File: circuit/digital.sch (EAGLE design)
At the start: 34 parts, among them IC1 MCP1701-5V, IC2 MCP1700-3.3V, X1 MINI-USB-SCHIELD-32005-301

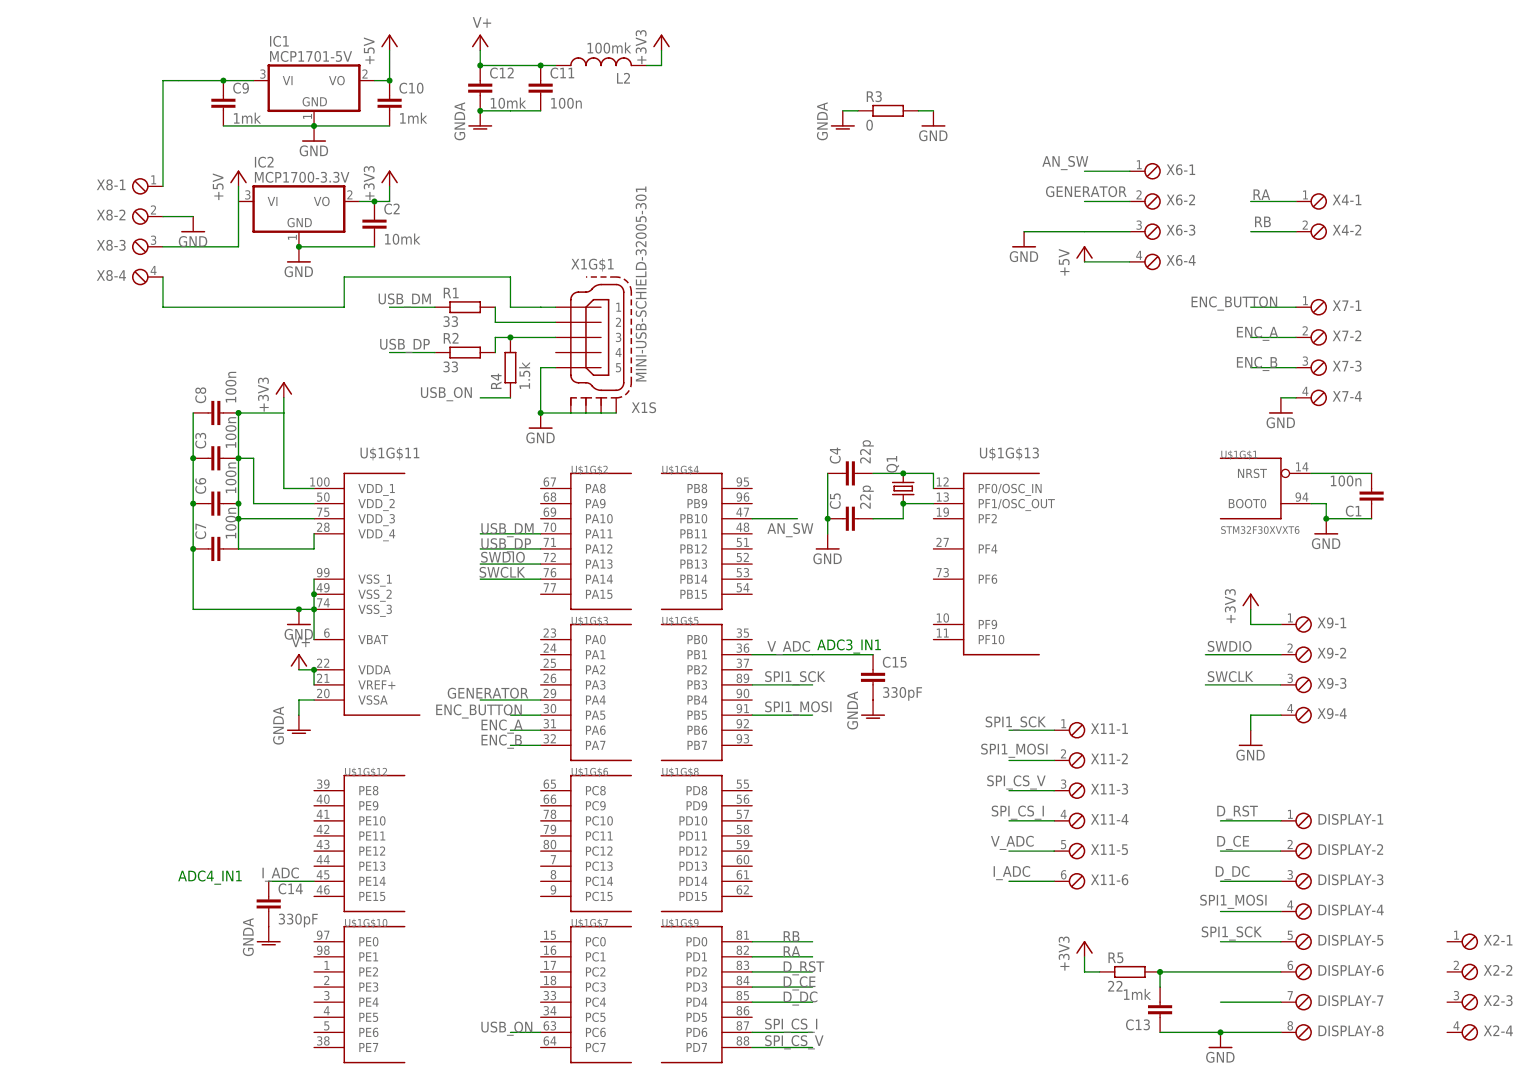
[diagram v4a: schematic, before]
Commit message: - слили вместе GND и GNDA - добавили измерение VBAT напряжения
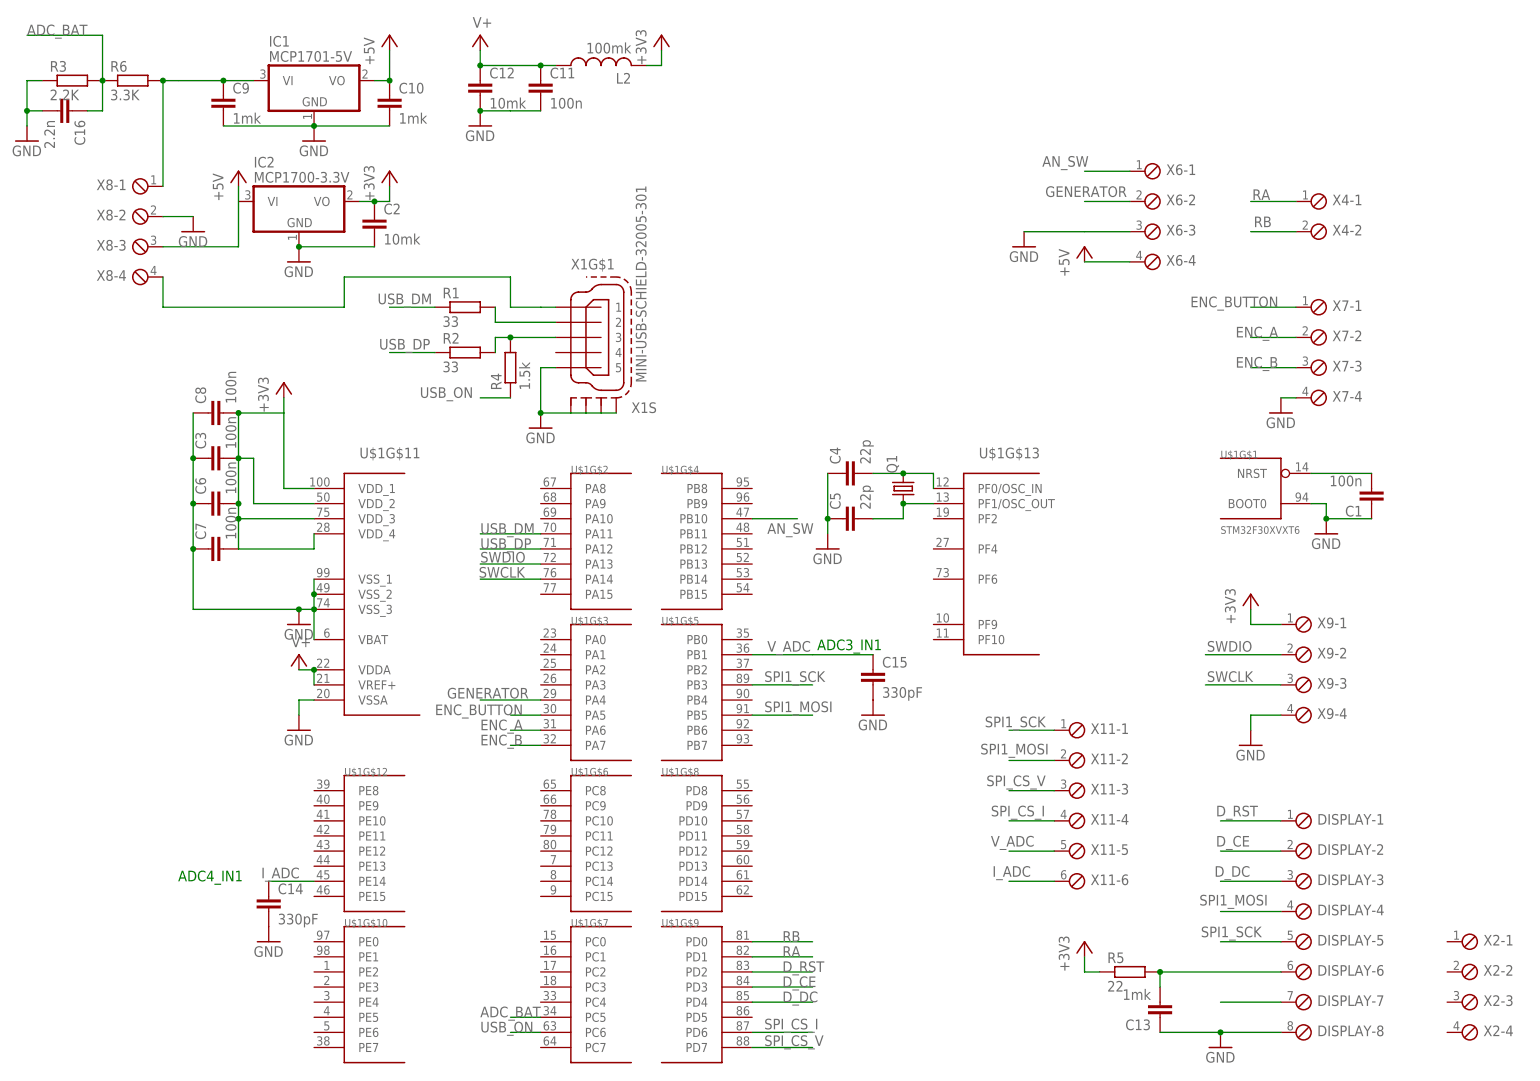
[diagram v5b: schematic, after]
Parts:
- added C16: 2.2n, rcl:C-EUC0805
- added R6: 3.3K, rcl:R-EU_R0603
- R3: value 0 -> 2.2K
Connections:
- removed net GNDA: C11.2, C12.2, C14.2, C15.2, R3.1, U$1G$11.VSSA
- new net ADC_BAT: C16.1, R3.2, R6.1, U$1G$7.PC5
- net GND: now also C11.2, C12.2, C14.2, C15.2, C16.2, R3.1, U$1G$11.VSSA; no longer R3.2
- net N$7: now also R6.2
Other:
- moved on the sheet: R3
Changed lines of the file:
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@@
 <part name="C11" library="rcl" deviceset="C-EU" device="C0603" value="100n"/>
 <part name="C12" library="rcl" deviceset="C-EU" device="C0805" value="10mk"/>
-<part name="GND10" library="supply1" deviceset="GNDA" device=""/>
 <part name="X4" library="con-phoenix-254" deviceset="MPT2" device=""/>
 <part name="SUPPLY1" library="supply2" deviceset="V+" device=""/>
@@
 <part name="C5" library="rcl" deviceset="C-EU" device="C0805" value="22p"/>
 <part name="GND5" library="supply1" deviceset="GND" device=""/>
-<part name="GND6" library="supply1" deviceset="GNDA" device=""/>
 <part name="SUPPLY2" library="supply2" deviceset="V+" device=""/>
 <part name="GND7" library="supply1" deviceset="GND" device=""/>
@@
 <part name="+3V3" library="supply1" deviceset="+3V3" device=""/>
 <part name="GND8" library="supply1" deviceset="GND" device=""/>
-<part name="GND9" library="supply1" deviceset="GNDA" device=""/>
-<part name="R3" library="rcl" deviceset="R-EU_" device="R0603" value="0"/>
 <part name="GND11" library="supply1" deviceset="GND" device=""/>
 <part name="C9" library="rcl" deviceset="C-EU" device="C0603" value="1mk"/>
@@
 <part name="R5" library="rcl" deviceset="R-EU_" device="R0603" value="22"/>
 <part name="C14" library="rcl" deviceset="C-EU" device="C0805" value="330pF"/>
-<part name="GND14" library="supply1" deviceset="GNDA" device=""/>
 <part name="C15" library="rcl" deviceset="C-EU" device="C0805" value="330pF"/>
-<part name="GND15" library="supply1" deviceset="GNDA" device=""/>
 <part name="X6" library="con-phoenix-254" deviceset="MPT4" device=""/>
 <part name="P+3" library="supply1" deviceset="+5V" device=""/>
@@
 <part name="X8" library="con-phoenix-254" deviceset="MPT4" device=""/>
 <part name="GND17" library="supply1" deviceset="GND" device=""/>
+<part name="GND6" library="supply1" deviceset="GND" device=""/>
+<part name="GND9" library="supply1" deviceset="GND" device=""/>
+<part name="GND10" library="supply1" deviceset="GND" device=""/>
+<part name="R3" library="rcl" deviceset="R-EU_" device="R0603" value="2.2K"/>
+<part name="R6" library="rcl" deviceset="R-EU_" device="R0603" value="3.3K"/>
+<part name="GND14" library="supply1" deviceset="GND" device=""/>
+<part name="C16" library="rcl" deviceset="C-EU" device="C0805" value="2.2n"/>
 </parts>
 <sheets>
@@
 <instance part="C11" gate="G$1" x="50.8" y="96.52"/>
 <instance part="C12" gate="G$1" x="40.64" y="96.52"/>
-<instance part="GND10" gate="1" x="40.64" y="88.9"/>
 <instance part="X4" gate="-1" x="180.34" y="76.2"/>
 <instance part="X4" gate="-2" x="180.34" y="71.12"/>
@@
 <instance part="C5" gate="G$1" x="101.6" y="22.86" rot="R90"/>
 <instance part="GND5" gate="1" x="99.06" y="17.78"/>
-<instance part="GND6" gate="1" x="10.16" y="-12.7"/>
 <instance part="SUPPLY2" gate="1" x="10.16" y="0"/>
 <instance part="GND7" gate="1" x="10.16" y="5.08"/>
@@
 <instance part="C8" gate="G$1" x="-5.08" y="40.64" rot="R90"/>
 <instance part="+3V3" gate="G$1" x="7.62" y="45.72"/>
-<instance part="GND8" gate="1" x="116.84" y="88.9"/>
-<instance part="GND9" gate="1" x="101.6" y="88.9"/>
-<instance part="R3" gate="G$1" x="109.22" y="91.44"/>
+<instance part="GND8" gate="1" x="40.64" y="88.9"/>
 <instance part="GND11" gate="1" x="12.7" y="86.36"/>
 <instance part="C9" gate="G$1" x="-2.54" y="93.98"/>
@@
 <instance part="R5" gate="G$1" x="149.86" y="-53.34"/>
 <instance part="C14" gate="G$1" x="5.08" y="-40.64"/>
-<instance part="GND14" gate="1" x="5.08" y="-48.26"/>
 <instance part="C15" gate="G$1" x="106.68" y="-2.54"/>
-<instance part="GND15" gate="1" x="106.68" y="-10.16"/>
 <instance part="X6" gate="-1" x="152.4" y="81.28"/>
 <instance part="X6" gate="-2" x="152.4" y="76.2"/>
@@
 <instance part="X8" gate="-4" x="-15.24" y="63.5" rot="MR0"/>
 <instance part="GND17" gate="1" x="-7.62" y="71.12"/>
+<instance part="GND6" gate="1" x="5.08" y="-48.26"/>
+<instance part="GND9" gate="1" x="106.68" y="-10.16"/>
+<instance part="GND10" gate="1" x="10.16" y="-12.7"/>
+<instance part="R3" gate="G$1" x="-27.94" y="96.52"/>
+<instance part="R6" gate="G$1" x="-17.78" y="96.52"/>
+<instance part="GND14" gate="1" x="-35.56" y="86.36"/>
+<instance part="C16" gate="G$1" x="-27.94" y="91.44" rot="R270"/>
 </instances>
 <busses>
@@
 <wire x1="149.86" y1="66.04" x2="142.24" y2="66.04" width="0.1524" layer="91"/>
 <pinref part="P+3" gate="1" pin="+5V"/>
-</segment>
-</net>
-<net name="GNDA" class="0">
-<segment>
-<pinref part="C11" gate="G$1" pin="2"/>
-<wire x1="45.72" y1="91.44" x2="50.8" y2="91.44" width="0.1524" layer="91"/>
-<pinref part="C12" gate="G$1" pin="2"/>
-<wire x1="40.64" y1="91.44" x2="45.72" y2="91.44" width="0.1524" layer="91"/>
-<pinref part="GND10" gate="1" pin="GNDA"/>
-<junction x="40.64" y="91.44"/>
-</segment>
-<segment>
-<pinref part="U$1" gate="G$11" pin="VSSA"/>
-<pinref part="GND6" gate="1" pin="GNDA"/>
-<wire x1="12.7" y1="-7.62" x2="10.16" y2="-7.62" width="0.1524" layer="91"/>
-<wire x1="10.16" y1="-7.62" x2="10.16" y2="-10.16" width="0.1524" layer="91"/>
-</segment>
-<segment>
-<pinref part="GND9" gate="1" pin="GNDA"/>
-<pinref part="R3" gate="G$1" pin="1"/>
-<wire x1="101.6" y1="91.44" x2="104.14" y2="91.44" width="0.1524" layer="91"/>
-</segment>
-<segment>
-<pinref part="C14" gate="G$1" pin="2"/>
-<pinref part="GND14" gate="1" pin="GNDA"/>
-</segment>
-<segment>
-<pinref part="C15" gate="G$1" pin="2"/>
-<pinref part="GND15" gate="1" pin="GNDA"/>
 </segment>
 </net>
@@
 </segment>
 <segment>
-<pinref part="GND8" gate="1" pin="GND"/>
-<pinref part="R3" gate="G$1" pin="2"/>
-<wire x1="116.84" y1="91.44" x2="114.3" y2="91.44" width="0.1524" layer="91"/>
-</segment>
-<segment>
 <pinref part="IC1" gate="G$1" pin="GND"/>
 <pinref part="GND11" gate="1" pin="GND"/>
@@
 <pinref part="X8" gate="-2" pin="1"/>
 <wire x1="-7.62" y1="73.66" x2="-12.7" y2="73.66" width="0.1524" layer="91"/>
+</segment>
+<segment>
+<pinref part="C11" gate="G$1" pin="2"/>
+<wire x1="45.72" y1="91.44" x2="50.8" y2="91.44" width="0.1524" layer="91"/>
+<pinref part="C12" gate="G$1" pin="2"/>
+<wire x1="40.64" y1="91.44" x2="45.72" y2="91.44" width="0.1524" layer="91"/>
+<pinref part="GND8" gate="1" pin="GND"/>
+<junction x="40.64" y="91.44"/>
+</segment>
+<segment>
+<pinref part="C14" gate="G$1" pin="2"/>
+<pinref part="GND6" gate="1" pin="GND"/>
+</segment>
+<segment>
+<pinref part="C15" gate="G$1" pin="2"/>
+<pinref part="GND9" gate="1" pin="GND"/>
+</segment>
+<segment>
+<pinref part="U$1" gate="G$11" pin="VSSA"/>
+<wire x1="12.7" y1="-7.62" x2="10.16" y2="-7.62" width="0.1524" layer="91"/>
+<wire x1="10.16" y1="-7.62" x2="10.16" y2="-10.16" width="0.1524" layer="91"/>
+<pinref part="GND10" gate="1" pin="GND"/>
+</segment>
+<segment>
+<pinref part="R3" gate="G$1" pin="1"/>
+<pinref part="GND14" gate="1" pin="GND"/>
+<wire x1="-33.02" y1="96.52" x2="-35.56" y2="96.52" width="0.1524" layer="91"/>
+<wire x1="-35.56" y1="96.52" x2="-35.56" y2="91.44" width="0.1524" layer="91"/>
+<pinref part="C16" gate="G$1" pin="2"/>
+<wire x1="-35.56" y1="91.44" x2="-35.56" y2="88.9" width="0.1524" layer="91"/>
+<wire x1="-33.02" y1="91.44" x2="-35.56" y2="91.44" width="0.1524" layer="91"/>
+<junction x="-35.56" y="91.44"/>
 </segment>
 </net>
@@
 <wire x1="-10.16" y1="96.52" x2="-12.7" y2="96.52" width="0.1524" layer="91"/>
 <wire x1="-12.7" y1="96.52" x2="-12.7" y2="78.74" width="0.1524" layer="91"/>
+<pinref part="R6" gate="G$1" pin="2"/>
+<junction x="-12.7" y="96.52"/>
 </segment>
 </net>
@@
 </segment>
 </net>
+<net name="ADC_BAT" class="0">
+<segment>
+<pinref part="R6" gate="G$1" pin="1"/>
+<pinref part="R3" gate="G$1" pin="2"/>
+<wire x1="-22.86" y1="96.52" x2="-22.86" y2="104.14" width="0.1524" layer="91"/>
+<wire x1="-22.86" y1="104.14" x2="-35.56" y2="104.14" width="0.1524" layer="91"/>
+<label x="-35.56" y="104.14" size="1.778" layer="95"/>
+<junction x="-22.86" y="96.52"/>
+<wire x1="-22.86" y1="96.52" x2="-22.86" y2="91.44" width="0.1524" layer="91"/>
+<pinref part="C16" gate="G$1" pin="1"/>
+<wire x1="-22.86" y1="91.44" x2="-25.4" y2="91.44" width="0.1524" layer="91"/>
+</segment>
+<segment>
+<pinref part="U$1" gate="G$7" pin="PC5"/>
+<wire x1="50.8" y1="-60.96" x2="45.72" y2="-60.96" width="0.1524" layer="91"/>
+<label x="40.64" y="-60.96" size="1.778" layer="95"/>
+</segment>
+</net>

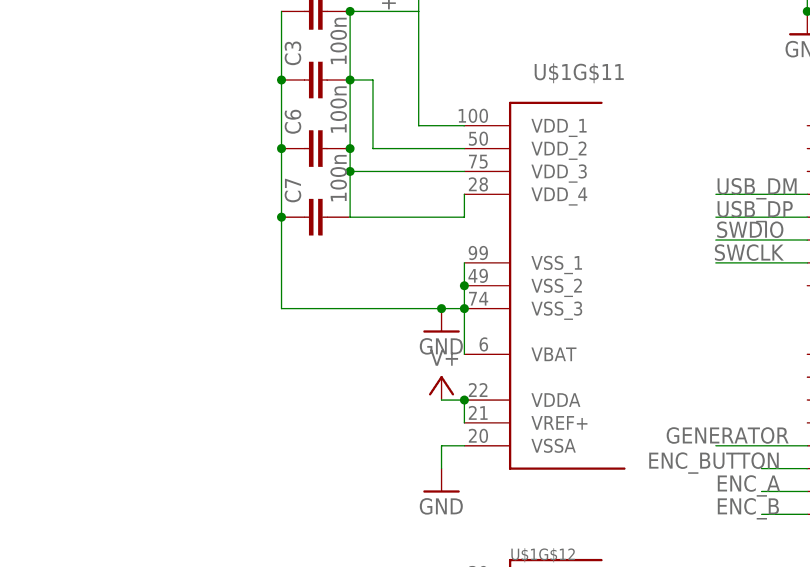
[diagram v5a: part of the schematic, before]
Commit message: - Vbat таки подключать к питанию, а не к земле
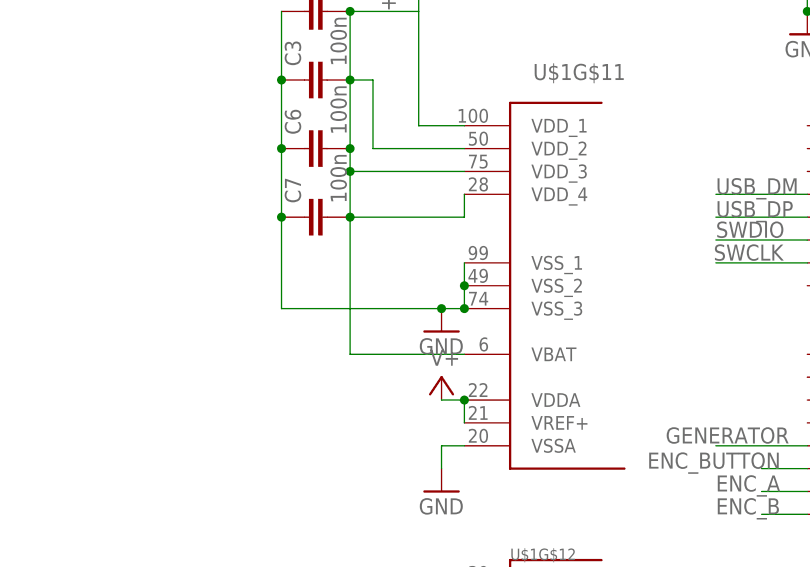
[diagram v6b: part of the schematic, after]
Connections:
- net +3V3: now also U$1G$11.VBAT
- net GND: no longer U$1G$11.VBAT
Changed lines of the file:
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@@
 <junction x="-7.62" y="25.4"/>
 <junction x="-7.62" y="33.02"/>
-<pinref part="U$1" gate="G$11" pin="VBAT"/>
-<wire x1="12.7" y1="2.54" x2="12.7" y2="7.62" width="0.1524" layer="91"/>
 </segment>
 <segment>
@@
 <junction x="0" y="33.02"/>
 <junction x="0" y="40.64"/>
+<pinref part="U$1" gate="G$11" pin="VBAT"/>
+<wire x1="12.7" y1="2.54" x2="0" y2="2.54" width="0.1524" layer="91"/>
+<wire x1="0" y1="2.54" x2="0" y2="17.78" width="0.1524" layer="91"/>
+<junction x="0" y="17.78"/>
 </segment>
 <segment>

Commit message: - завели софтварный SPI1
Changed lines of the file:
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@@
 <pinref part="X8" gate="-3" pin="1"/>
 <wire x1="0" y1="68.58" x2="-12.7" y2="68.58" width="0.1524" layer="91"/>
+<junction x="0" y="76.2"/>
 </segment>
 <segment>
@@
 <wire x1="0" y1="2.54" x2="0" y2="17.78" width="0.1524" layer="91"/>
 <junction x="0" y="17.78"/>
-</segment>
-<segment>
+<junction x="7.62" y="40.64"/>
+</segment>
+<segment>

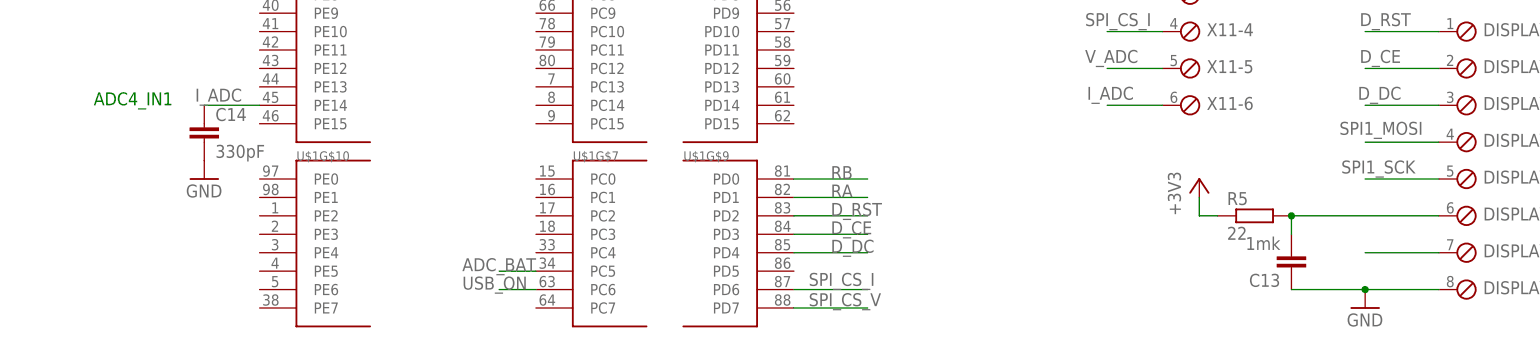
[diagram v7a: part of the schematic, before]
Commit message: Нарисовал таки PE1 - управление backlight
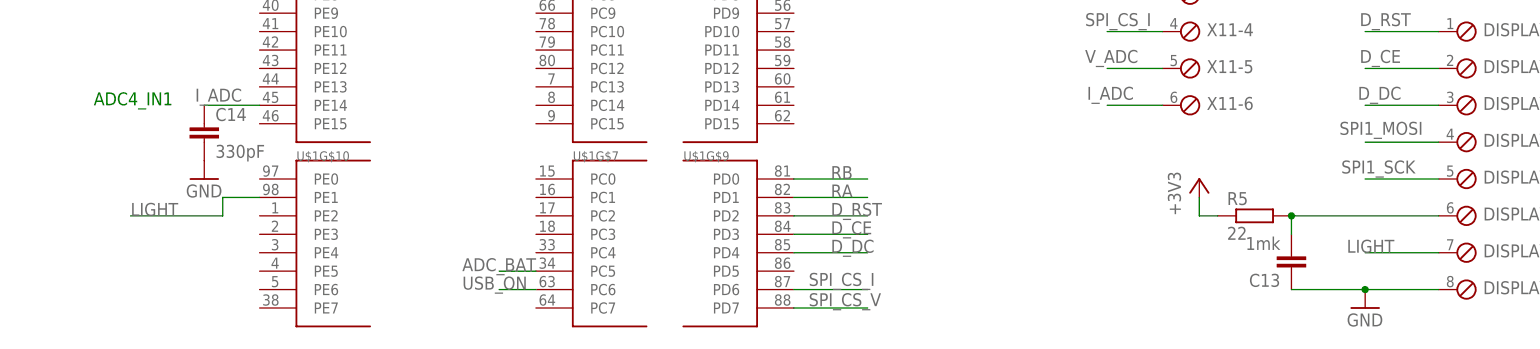
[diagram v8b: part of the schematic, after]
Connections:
- removed net N$13: DISPLAY-7.1
- new net LIGHT: DISPLAY-7.1, U$1G$10.PE1
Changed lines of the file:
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@@
 <?xml version="1.0" encoding="utf-8"?>
 <!DOCTYPE eagle SYSTEM "eagle.dtd">
-<eagle version="6.5.0">
+<eagle version="7.4.0">
 <drawing>
 <settings>
@@
 </segment>
 </net>
-<net name="N$13" class="0">
+<net name="LIGHT" class="0">
 <segment>
 <pinref part="DISPLAY" gate="-7" pin="1"/>
 <wire x1="175.26" y1="-58.42" x2="165.1" y2="-58.42" width="0.1524" layer="91"/>
-</segment>
-</net>
+<label x="162.56" y="-58.42" size="1.778" layer="95"/>
+</segment>
+<segment>
+<pinref part="U$1" gate="G$10" pin="PE1"/>
+<wire x1="12.7" y1="-50.8" x2="7.62" y2="-50.8" width="0.1524" layer="91"/>
+<wire x1="7.62" y1="-50.8" x2="7.62" y2="-53.34" width="0.1524" layer="91"/>
+<wire x1="7.62" y1="-53.34" x2="-5.08" y2="-53.34" width="0.1524" layer="91"/>
+<label x="-5.08" y="-53.34" size="1.778" layer="95"/>
+</segment>
+</net>
